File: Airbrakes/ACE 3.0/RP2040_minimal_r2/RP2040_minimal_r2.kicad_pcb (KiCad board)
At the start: 2 copper layers, 52 x 51 mm, 44 parts, among them J1 USB_B_Micro, J2 Conn_01x02, J3 104031-0811, J4 Conn_02x18_Odd_Even, U1 NCP1117-3.3_SOT223, U2 W25Q128JVS, U3 RP2040, U4 BMI088, U5 BMP581, U6 BMM350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

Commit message: Update traces
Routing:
- net +3V3: track 61.6 -> 62.3 mm
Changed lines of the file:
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@@
+	)
+	(segment
+		(start 92.475 99.717463)
+		(end 92.782537 100.025)
+		(width 0.15)
+		(layer "F.Cu")
+		(net 5)
 	)
 	(segment
@@
 	)
 	(segment
-		(start 95.6 97.4)
-		(end 94 99)
-		(width 0.2)
-		(layer "F.Cu")
-		(net 5)
-	)
-	(segment
 		(start 100.2 95.7)
 		(end 100.2 96.5625)
@@
 	)
 	(segment
+		(start 92.782537 100.025)
+		(end 93.475 100.025)
+		(width 0.15)
+		(layer "F.Cu")
+		(net 5)
+	)
+	(segment
 		(start 100.350001 94.112535)
 		(end 100.350001 95.549999)
@@
 	)
 	(segment
-		(start 93.5 100)
-		(end 93.475 100)
-		(width 0.2)
-		(layer "F.Cu")
-		(net 5)
-	)
-	(segment
 		(start 93 112.5)
 		(end 93 112)
@@
 	)
 	(segment
+		(start 96.1 97.4)
+		(end 96.5625 97.4)
+		(width 0.15)
+		(layer "F.Cu")
+		(net 5)
+	)
+	(segment
 		(start 100.6 96.5625)
 		(end 100.6 97.2)
@@
 	)
 	(segment
-		(start 92.782537 100.025)
-		(end 93.475 100.025)
-		(width 0.15)
-		(layer "F.Cu")
-		(net 5)
-	)
-	(segment
 		(start 88.905 81.805)
 		(end 89.5 81.805)
@@
 	)
 	(segment
+		(start 80.805 97.805)
+		(end 81.605 98.605)
+		(width 0.15)
+		(layer "F.Cu")
+		(net 5)
+	)
+	(segment
+		(start 80.05 97.805)
+		(end 80.805 97.805)
+		(width 0.15)
+		(layer "F.Cu")
+		(net 5)
+	)
+	(segment
 		(start 100.6 96.5625)
 		(end 100.6 95.799998)
@@
 	)
 	(segment
-		(start 94 99)
-		(end 94 99.5)
+		(start 100.2 96.5625)
+		(end 100.2 97.4)
+		(width 0.2)
+		(layer "F.Cu")
+		(net 5)
+	)
+	(segment
+		(start 108 86)
+		(end 108 89)
+		(width 0.2)
+		(layer "F.Cu")
+		(net 5)
+	)
+	(segment
+		(start 100.381 105.6865)
+		(end 100.381 106)
+		(width 0.2)
+		(layer "F.Cu")
+		(net 5)
+	)
+	(segment
+		(start 100.350001 95.549999)
+		(end 100.2 95.7)
+		(width 0.2)
+		(layer "F.Cu")
+		(net 5)
+	)
+	(segment
+		(start 80.05 97.805)
+		(end 79.805 97.805)
+		(width 0.15)
+		(layer "F.Cu")
+		(net 5)
+	)
+	(segment
+		(start 102.2 96.1)
+		(end 103.6 94.7)
+		(width 0.2)
+		(layer "F.Cu")
+		(net 5)
+	)
+	(segment
+		(start 92.81 109.15)
+		(end 93.46 108.5)
+		(width 0.15)
+		(layer "F.Cu")
+		(net 5)
+	)
+	(segment
+		(start 100.2 97.4)
+		(end 100.2 97)
+		(width 0.2)
+		(layer "F.Cu")
+		(net 5)
+	)
+	(segment
+		(start 81.605 98.605)
+		(end 91.694332 98.605)
+		(width 0.15)
+		(layer "F.Cu")
+		(net 5)
+	)
+	(segment
+		(start 100 93.762534)
+		(end 100.350001 94.112535)
+		(width 0.2)
+		(layer "F.Cu")
+		(net 5)
+	)
+	(segment
+		(start 93.475 100.025)
+		(end 96.1 97.4)
+		(width 0.15)
+		(layer "F.Cu")
+		(net 5)
+	)
+	(segment
+		(start 92 109.67)
+		(end 92 109.225)
+		(width 0.15)
+		(layer "F.Cu")
+		(net 5)
+	)
+	(segment
+		(start 96.65 85.37)
+		(end 96.65 82.85)
+		(width 0.2)
+		(layer "F.Cu")
+		(net 5)
+	)
+	(segment
+		(start 100.2 103.4375)
+		(end 100.2 102.8)
+		(width 0.2)
+		(layer "F.Cu")
+		(net 5)
+	)
+	(segment
+		(start 102.2 96.5625)
+		(end 102.2 96.1)
+		(width 0.2)
+		(layer "F.Cu")
+		(net 5)
+	)
+	(segment
+		(start 96.65 82.85)
+		(end 96.67 82.83)
 		(width 0.2)
 		(layer "F.Cu")
@@
 		(layer "F.Cu")
 		(net 5)
-	)
-	(segment
-		(start 100.2 96.5625)
-		(end 100.2 97.4)
-		(width 0.2)
-		(layer "F.Cu")
-		(net 5)
-	)
-	(segment
-		(start 108 86)
-		(end 108 89)
-		(width 0.2)
-		(layer "F.Cu")
-		(net 5)
-	)
-	(segment
-		(start 100.381 105.6865)
-		(end 100.381 106)
-		(width 0.2)
-		(layer "F.Cu")
-		(net 5)
-	)
-	(segment
-		(start 94 99.5)
-		(end 93.5 100)
-		(width 0.2)
-		(layer "F.Cu")
-		(net 5)
-	)
-	(segment
-		(start 92.475 99.717463)
-		(end 92.782537 100.025)
-		(width 0.15)
-		(layer "F.Cu")
-		(net 5)
-	)
-	(segment
-		(start 100.350001 95.549999)
-		(end 100.2 95.7)
-		(width 0.2)
-		(layer "F.Cu")
-		(net 5)
-	)
-	(segment
-		(start 80.05 97.805)
-		(end 79.805 97.805)
-		(width 0.15)
-		(layer "F.Cu")
-		(net 5)
-	)
-	(segment
-		(start 102.2 96.1)
-		(end 103.6 94.7)
-		(width 0.2)
-		(layer "F.Cu")
-		(net 5)
-	)
-	(segment
-		(start 92.81 109.15)
-		(end 93.46 108.5)
-		(width 0.15)
-		(layer "F.Cu")
-		(net 5)
-	)
-	(segment
-		(start 81.605 98.605)
-		(end 91.694332 98.605)
-		(width 0.15)
-		(layer "F.Cu")
-		(net 5)
-	)
-	(segment
-		(start 80.805 97.805)
-		(end 81.605 98.605)
-		(width 0.15)
-		(layer "F.Cu")
-		(net 5)
-	)
-	(segment
-		(start 100.2 97.4)
-		(end 100.2 97)
-		(width 0.2)
-		(layer "F.Cu")
-		(net 5)
-	)
-	(segment
-		(start 100 93.762534)
-		(end 100.350001 94.112535)
-		(width 0.2)
-		(layer "F.Cu")
-		(net 5)
-	)
-	(segment
-		(start 80.05 97.805)
-		(end 80.805 97.805)
-		(width 0.15)
-		(layer "F.Cu")
-		(net 5)
-	)
-	(segment
-		(start 92 109.67)
-		(end 92 109.225)
-		(width 0.15)
-		(layer "F.Cu")
-		(net 5)
-	)
-	(segment
-		(start 96.65 85.37)
-		(end 96.65 82.85)
-		(width 0.2)
-		(layer "F.Cu")
-		(net 5)
-	)
-	(segment
-		(start 100.2 103.4375)
-		(end 100.2 102.8)
-		(width 0.2)
-		(layer "F.Cu")
-		(net 5)
-	)
-	(segment
-		(start 102.2 96.5625)
-		(end 102.2 96.1)
-		(width 0.2)
-		(layer "F.Cu")
-		(net 5)
-	)
-	(segment
-		(start 96.65 82.85)
-		(end 96.67 82.83)
-		(width 0.2)
-		(layer "F.Cu")
-		(net 5)

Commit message: Updated traces
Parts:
- moved J3 3.50 mm to (82.0, 98.0)
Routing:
- net GND: track 79.7 -> 99.5 mm
- net /MISO: track 21.8 -> 26.1 mm
- net +3V3: track 62.3 -> 65.6 mm
- net /MOSI: track 17.4 -> 20.7 mm
- net /CS_SD: track 26.3 -> 28.3 mm
- net /SCLK: track 29.9 -> 32.0 mm

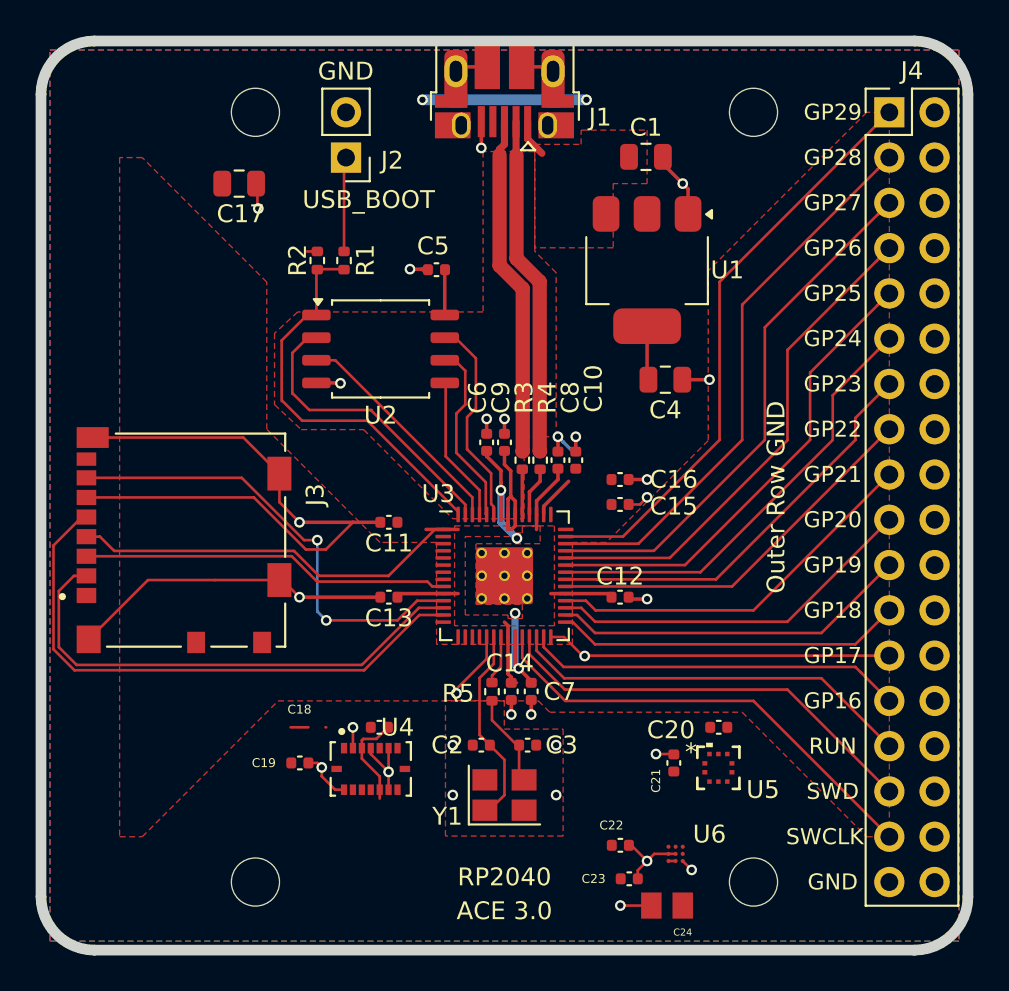
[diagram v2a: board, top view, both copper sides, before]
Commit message: Redraw left power plane
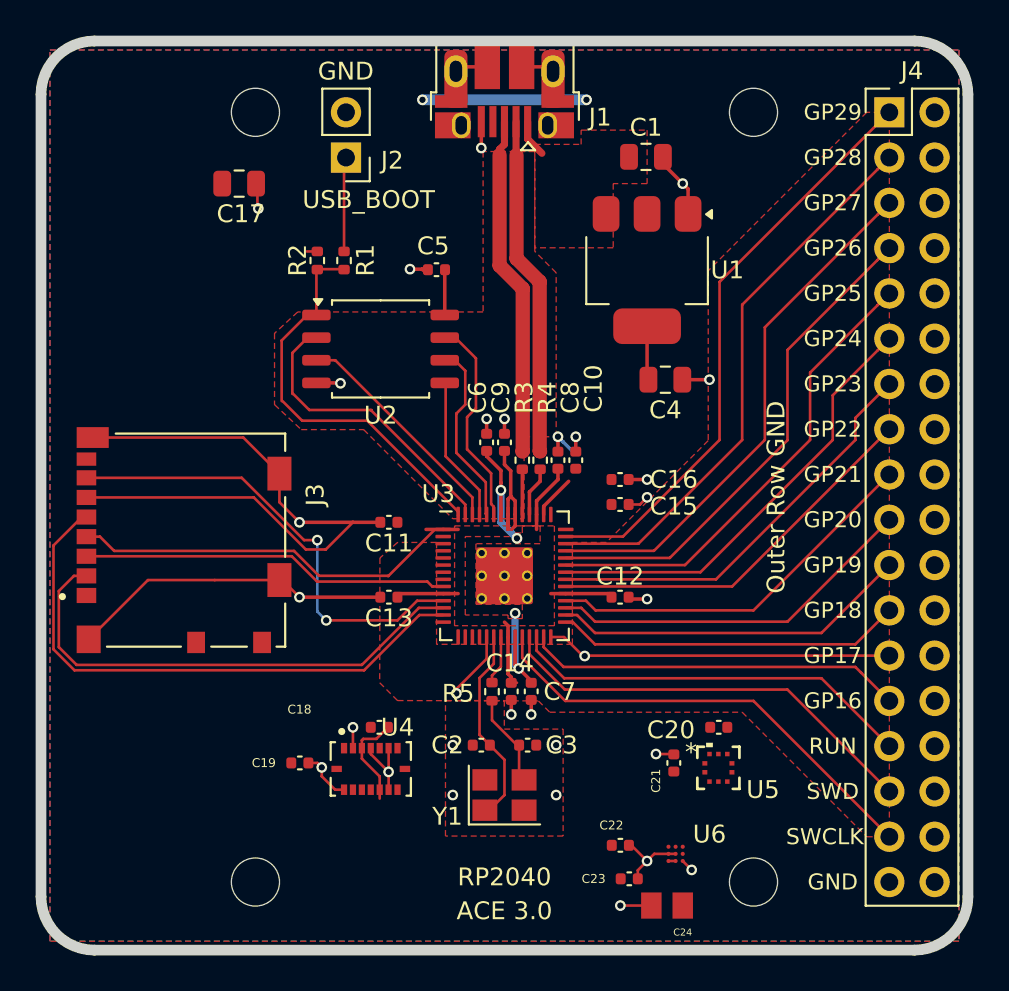
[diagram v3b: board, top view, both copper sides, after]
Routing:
- net GND: track 99.5 -> 98.5 mm
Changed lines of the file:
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@@
-	)
-	(segment
-		(start 89 108.5)
-		(end 88 108.5)
-		(width 0.15)
-		(layer "F.Cu")
-		(net 1)
 	)
 	(segment
@@
 		(start 92 109.67)
 		(end 92 110.257537)
-		(width 0.15)
-		(layer "F.Cu")
-		(net 5)
-	)
-	(segment
-		(start 89.96 108.5)
-		(end 90 108.5)
 		(width 0.15)
 		(layer "F.Cu")
@@
 			(pts
 				(xy 120.32 74) (xy 111.43 82.89) (xy 111.43 92.415) (xy 105.715 98.13) (xy 103.81 98.13) (xy 103.81 103.845)
-				(xy 96.19 103.845) (xy 96.19 98.13) (xy 93.015 98.13) (xy 86.665 91.78) (xy 86.665 83.525) (xy 79.68 76.54)
-				(xy 78.41 76.54) (xy 78.41 114.64) (xy 79.68 114.64) (xy 87.3 107.02) (xy 101.905 107.02) (xy 102.54 107.655)
-				(xy 113.335 107.655) (xy 120.32 114.64) (xy 121.59 114.64) (xy 121.59 74)
+				(xy 96.19 103.845) (xy 96.19 98.13) (xy 94 98.13) (xy 93.013229 99.000027) (xy 93 106) (xy 94 107)
+				(xy 101.905 107.02) (xy 102.54 107.655) (xy 113.335 107.655) (xy 120.32 114.64) (xy 121.59 114.64)
+				(xy 121.59 74)
 			)
 		)

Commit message: Update RP2040_minimal_r2.kicad_pcb
moved trace test
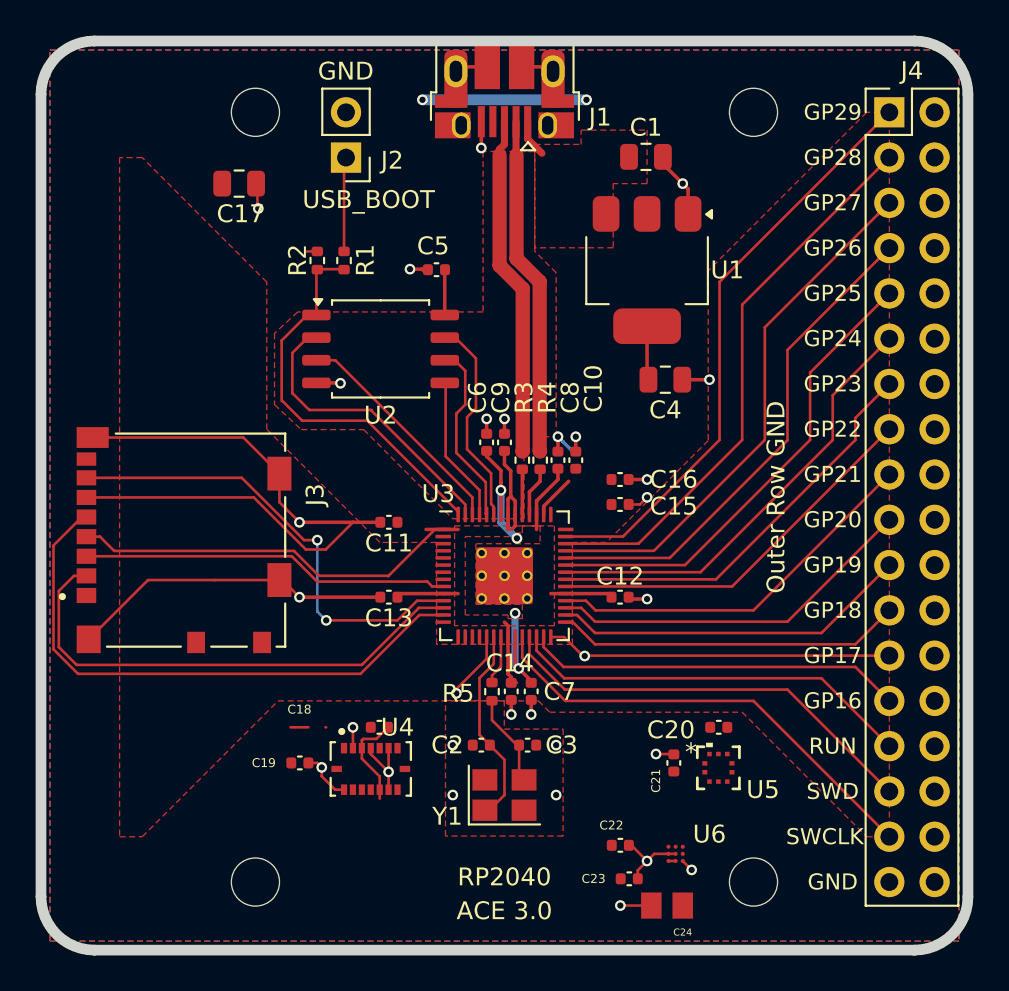
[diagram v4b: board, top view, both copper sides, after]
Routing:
- net GND: track 98.5 -> 99.5 mm
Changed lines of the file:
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@@
+	)
+	(segment
+		(start 89 108.5)
+		(end 88 108.5)
+		(width 0.15)
+		(layer "F.Cu")
+		(net 1)
 	)
 	(segment
@@
 		(start 92 109.67)
 		(end 92 110.257537)
+		(width 0.15)
+		(layer "F.Cu")
+		(net 5)
+	)
+	(segment
+		(start 89.96 108.5)
+		(end 90 108.5)
 		(width 0.15)
 		(layer "F.Cu")
@@
 	)
 	(segment
+		(start 76.295 96.705)
+		(end 74.7 98.3)
+		(width 0.15)
+		(layer "F.Cu")
+		(net 58)
+	)
+	(segment
 		(start 74.7 104.124264)
-		(end 74.7 98.3)
+		(end 76.075736 105.5)
 		(width 0.15)
 		(layer "F.Cu")
@@
 	)
 	(segment
-		(start 92.124264 105.3)
-		(end 75.875736 105.3)
+		(start 91.924264 105.5)
+		(end 95.224264 102.2)
 		(width 0.15)
 		(layer "F.Cu")
@@
 	)
 	(segment
-		(start 75.875736 105.3)
+		(start 74.7 98.3)
 		(end 74.7 104.124264)
 		(width 0.15)
@@
 	)
 	(segment
-		(start 96.5625 102.2)
-		(end 95.224264 102.2)
+		(start 76.075736 105.5)
+		(end 91.924264 105.5)
 		(width 0.15)
 		(layer "F.Cu")
@@
 	)
 	(segment
-		(start 74.7 98.3)
+		(start 95.224264 102.2)
+		(end 96.5625 102.2)
+		(width 0.15)
+		(layer "F.Cu")
+		(net 58)
+	)
+	(segment
+		(start 76.55 96.705)
 		(end 76.295 96.705)
-		(width 0.15)
-		(layer "F.Cu")
-		(net 58)
-	)
-	(segment
-		(start 95.224264 102.2)
-		(end 92.124264 105.3)
-		(width 0.15)
-		(layer "F.Cu")
-		(net 58)
-	)
-	(segment
-		(start 76.295 96.705)
-		(end 76.55 96.705)
 		(width 0.15)
 		(layer "F.Cu")
@@
 			(pts
 				(xy 120.32 74) (xy 111.43 82.89) (xy 111.43 92.415) (xy 105.715 98.13) (xy 103.81 98.13) (xy 103.81 103.845)
-				(xy 96.19 103.845) (xy 96.19 98.13) (xy 94 98.13) (xy 93.013229 99.000027) (xy 93 106) (xy 94 107)
-				(xy 101.905 107.02) (xy 102.54 107.655) (xy 113.335 107.655) (xy 120.32 114.64) (xy 121.59 114.64)
-				(xy 121.59 74)
+				(xy 96.19 103.845) (xy 96.19 98.13) (xy 93.015 98.13) (xy 86.665 91.78) (xy 86.665 83.525) (xy 79.68 76.54)
+				(xy 78.41 76.54) (xy 78.41 114.64) (xy 79.68 114.64) (xy 87.3 107.02) (xy 101.905 107.02) (xy 102.54 107.655)
+				(xy 113.335 107.655) (xy 120.32 114.64) (xy 121.59 114.64) (xy 121.59 74)
 			)
 		)

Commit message: loose wire test
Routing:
- net (no net): track 0.00 -> 2.71 mm
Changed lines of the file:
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@@
+	)
+	(segment
+		(start 83.5 89.5)
+		(end 84 90)
+		(width 0.15)
+		(layer "F.Cu")
+		(net 0)
+	)
+	(segment
+		(start 81.5 89.5)
+		(end 83.5 89.5)
+		(width 0.15)
+		(layer "F.Cu")
+		(net 0)
 	)
 	(segment
